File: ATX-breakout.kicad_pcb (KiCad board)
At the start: 2 copper layers, 67 x 59.5 mm, 27 parts, among them J1 I2C, J10 3V3 out, J11 12V out, J12 12V out, J2 EPS, J3 USB_A, J4 Raspberry_Pi_2_3, J5 ATX24pin, J6 12V out, J7 pson ext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

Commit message: added schematic PDF and updated BOM
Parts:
- R2: value 10K -> 10k
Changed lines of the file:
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@@
       (effects (font (size 1 1) (thickness 0.15)))
     )
-    (fp_text value 10K (at 3.81 2.37) (layer F.Fab)
+    (fp_text value 10k (at 3.81 2.37) (layer F.Fab)
       (effects (font (size 1 1) (thickness 0.15)))
     )

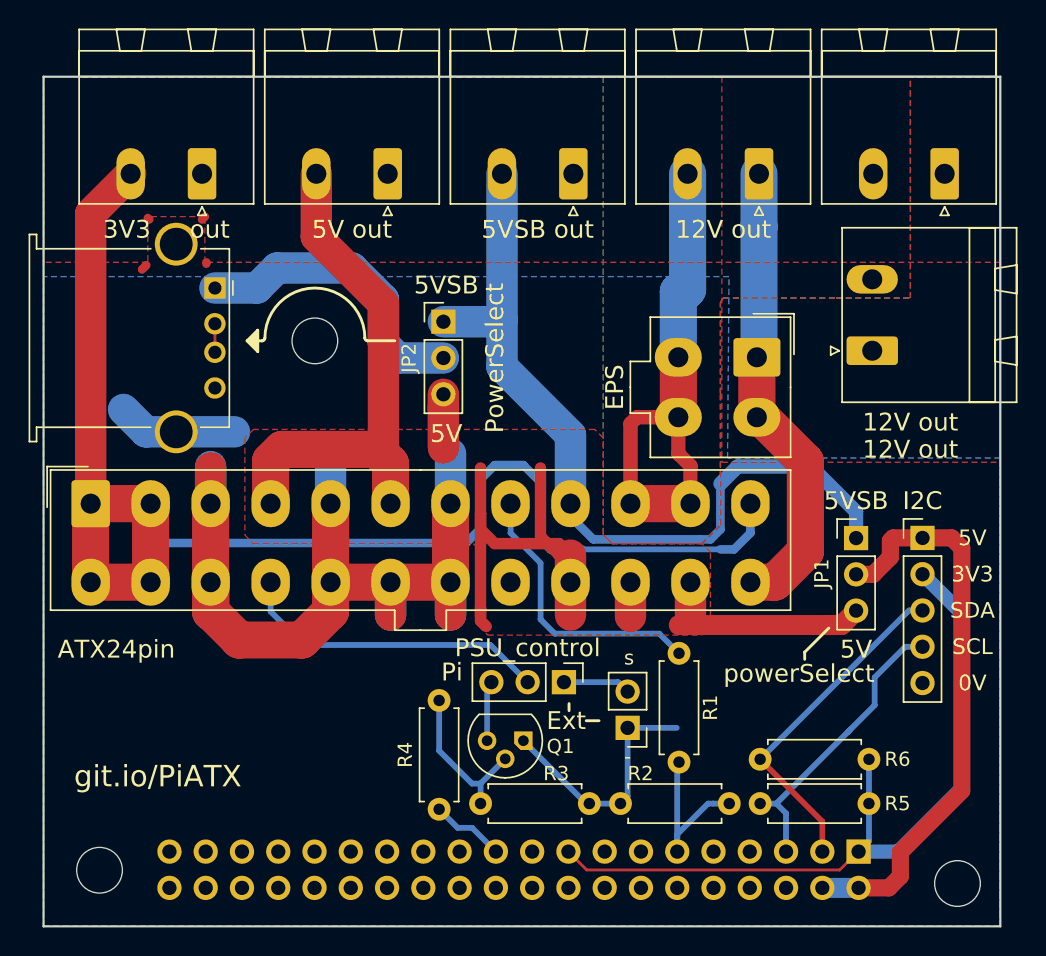
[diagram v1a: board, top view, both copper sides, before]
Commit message: rotated EPS and improved ground routing
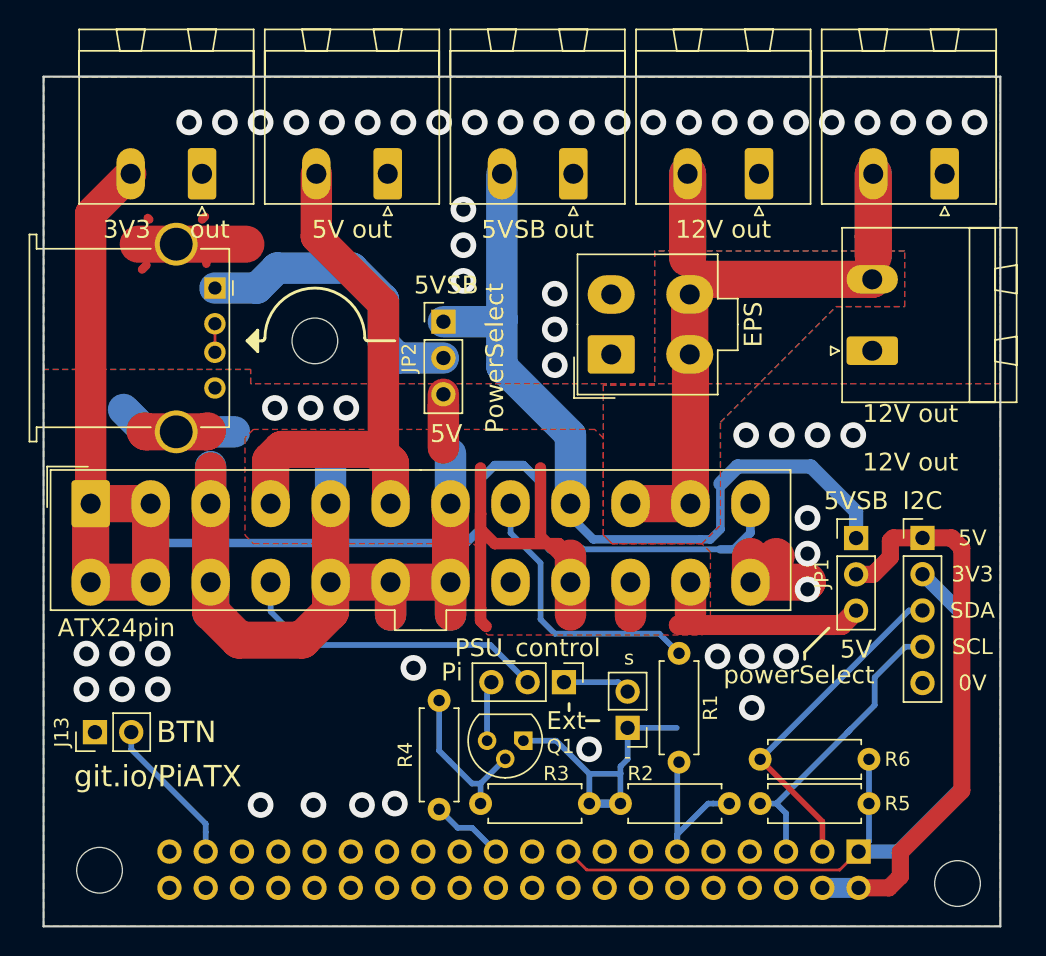
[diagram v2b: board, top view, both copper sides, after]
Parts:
- added J13: btn, Connector_PinHeader_2.54mm:PinHeader_1x02_P2.54mm_Vertical, F.Cu at (3.60, 45.9)
- moved J2 10.2 mm to (39.8, 19.4), turned to 90 degrees
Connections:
- J4 pad 37: (no net) -> Net-(J13-Pad2)
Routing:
- net +12V: track 37.4 -> 55.4 mm
- net Net-(J13-Pad2): track 0.00 -> 10.5 mm
- net GND: track 124.2 -> 115.1 mm, vias 0 -> 55
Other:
- board text added: "BTN"

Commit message: Updated silk screen and gerbers
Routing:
- net GND: vias 55 -> 54
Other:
- board text added: "GND"
- board text added: "PowerSelect USB"
- board text added: "powerSelect RPi"
- board text removed: "0V"
- board text removed: "PowerSelect"
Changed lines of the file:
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@@
   (general
     (thickness 1.6)
-    (drawings 61)
-    (tracks 275)
+    (drawings 74)
+    (tracks 274)
     (zones 0)
     (modules 28)
@@
       (effects (font (size 1 1) (thickness 0.15)))
     )
-    (fp_text value powerSelect (at -4 9.59 180) (layer F.SilkS)
+    (fp_text value powerSelect (at -4 9.59 180) (layer F.SilkS) hide
       (effects (font (size 1.25 1.25) (thickness 0.2)))
     )
@@
       (effects (font (size 1 1) (thickness 0.15)))
     )
-    (fp_text value "12V out" (at 2.4 -16.8 180) (layer F.SilkS)
+    (fp_text value "12V out" (at 2.4 -17.2 180) (layer F.SilkS)
       (effects (font (size 1.25 1.25) (thickness 0.2)))
     )
@@
       (effects (font (size 1 1) (thickness 0.15)))
     )
-    (fp_text value "12V out" (at -7.81 2.67 180) (layer F.SilkS)
+    (fp_text value "12V out" (at -6.36 2.62 180) (layer F.SilkS)
       (effects (font (size 1.25 1.25) (thickness 0.2)))
     )
@@
     )
   )
+  (gr_line (start 58.9 34.85) (end 58.9 32.3) (layer F.SilkS) (width 0.2))
+  (gr_line (start 54.9 34.85) (end 54.9 37.4) (layer F.SilkS) (width 0.2))
+  (gr_line (start 56.9 34.85) (end 58.9 34.85) (layer F.SilkS) (width 0.2))
+  (gr_line (start 58.9 32.3) (end 56.9 32.3) (layer F.SilkS) (width 0.2))
+  (gr_line (start 56.9 34.85) (end 54.9 34.85) (layer F.SilkS) (width 0.2))
+  (gr_line (start 54.9 37.4) (end 56.9 37.4) (layer F.SilkS) (width 0.2))
+  (gr_line (start 26 19.7) (end 26 22.25) (layer F.SilkS) (width 0.2))
+  (gr_line (start 28 19.7) (end 26 19.7) (layer F.SilkS) (width 0.2))
+  (gr_line (start 26 22.25) (end 28 22.25) (layer F.SilkS) (width 0.2))
+  (gr_line (start 30 17.15) (end 28 17.15) (layer F.SilkS) (width 0.2))
+  (gr_line (start 30 19.7) (end 30 17.15) (layer F.SilkS) (width 0.2))
+  (gr_line (start 28 19.7) (end 30 19.7) (layer F.SilkS) (width 0.2))
+  (gr_text "powerSelect\nRPi" (at 52.9 42.95) (layer F.SilkS)
+    (effects (font (size 1.25 1.25) (thickness 0.2)))
+  )
   (gr_text BTN (at 10 45.9) (layer F.SilkS)
     (effects (font (size 1.5 1.5) (thickness 0.3)))
@@
     (effects (font (size 1 1) (thickness 0.15)) (justify mirror))
   )
-  (gr_text 0V (at 65.048 42.46) (layer F.SilkS)
+  (gr_text GND (at 65.048 42.46) (layer F.SilkS)
     (effects (font (size 1.1 1.1) (thickness 0.18)))
   )
@@
     (effects (font (size 1.25 1.25) (thickness 0.2)))
   )
-  (gr_text PowerSelect (at 31.6 19.7 90) (layer F.SilkS)
+  (gr_text "PowerSelect\nUSB" (at 32.75 19.7 90) (layer F.SilkS)
     (effects (font (size 1.25 1.25) (thickness 0.2)))
   )
@@
   (via (at 51.7 25.1) (size 1.8) (drill 1) (layers F.Cu B.Cu) (net 3))
   (via (at 54.2 25.1) (size 1.8) (drill 1) (layers F.Cu B.Cu) (net 3))
-  (via (at 56.7 25.1) (size 1.8) (drill 1) (layers F.Cu B.Cu) (net 3))
   (segment (start 53.45 35.4) (end 53.5 35.35) (width 2.6) (layer F.Cu) (net 3))
   (segment (start 49.5 35.4) (end 53.45 35.4) (width 2.6) (layer F.Cu) (net 3))

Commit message: updated gerbers, silkscreen and renders
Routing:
- net GND: track 115.1 -> 124.0 mm
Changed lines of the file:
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@@
   (general
     (thickness 1.6)
-    (drawings 74)
-    (tracks 274)
+    (drawings 75)
+    (tracks 278)
     (zones 0)
     (modules 28)
@@
   )
   (setup
-    (last_trace_width 0.4)
+    (last_trace_width 2.6)
     (user_trace_width 0.4)
     (user_trace_width 0.6)
@@
     (descr "Through hole straight pin header, 1x03, 2.54mm pitch, single row")
     (tags "Through hole pin header THT 1x03 2.54mm single row")
-    (fp_text reference JP1 (at -2.4 2.49 90) (layer F.SilkS)
+    (fp_text reference JP1 (at -2.4 -0.21 90) (layer F.SilkS)
       (effects (font (size 1 1) (thickness 0.15)))
     )
@@
     (descr "Through hole straight pin header, 1x03, 2.54mm pitch, single row")
     (tags "Through hole pin header THT 1x03 2.54mm single row")
-    (fp_text reference JP2 (at -2.4 2.54 90) (layer F.SilkS)
+    (fp_text reference JP2 (at -2.4 -0.01 90) (layer F.SilkS)
       (effects (font (size 1 1) (thickness 0.15)))
     )
@@
       (effects (font (size 1 1) (thickness 0.15)))
     )
-    (fp_text value "12V out" (at -6.36 2.62 180) (layer F.SilkS)
+    (fp_text value "12V out" (at -6.56 2.62 180) (layer F.SilkS)
       (effects (font (size 1.25 1.25) (thickness 0.2)))
     )
@@
     )
   )
+  (gr_text git.io/PiATX (at 8 49) (layer B.SilkS)
+    (effects (font (size 1.5 1.5) (thickness 0.3)) (justify mirror))
+  )
   (gr_line (start 58.9 34.85) (end 58.9 32.3) (layer F.SilkS) (width 0.2))
   (gr_line (start 54.9 34.85) (end 54.9 37.4) (layer F.SilkS) (width 0.2))
@@
     (effects (font (size 1 1) (thickness 0.15)) (justify mirror))
   )
-  (gr_text "(64, 56.5)" (at 64 49.5 90) (layer B.SilkS)
+  (gr_text "(64, 56.5)" (at 62.6 52.5) (layer B.SilkS)
     (effects (font (size 1 1) (thickness 0.15)) (justify mirror))
   )
@@
   (via (at 29.4 9.3) (size 1.8) (drill 1) (layers F.Cu B.Cu) (net 3))
   (via (at 29.4 11.8) (size 1.8) (drill 1) (layers F.Cu B.Cu) (net 3))
-  (via (at 29.4 14.3) (size 1.8) (drill 1) (layers F.Cu B.Cu) (net 3))
   (via (at 49.2 25.1) (size 1.8) (drill 1) (layers F.Cu B.Cu) (net 3))
   (via (at 51.7 25.1) (size 1.8) (drill 1) (layers F.Cu B.Cu) (net 3))
@@
   (via (at 18.9 51) (size 1.8) (drill 1) (layers F.Cu B.Cu) (net 3))
   (via (at 15.2 51) (size 1.8) (drill 1) (layers F.Cu B.Cu) (net 3))
+  (via (at 26.9 11.8) (size 1.8) (drill 1) (layers F.Cu B.Cu) (net 3))
+  (segment (start 53.45 35.4) (end 53.5 35.35) (width 2.6) (layer B.Cu) (net 3))
+  (segment (start 49.5 35.4) (end 51.3 33.6) (width 2.6) (layer B.Cu) (net 3))
+  (segment (start 49.5 35.4) (end 53.45 35.4) (width 2.6) (layer B.Cu) (net 3))
+  (segment (start 49.5 35.4) (end 49.5 37.7) (width 2.6) (layer B.Cu) (net 3))
   (segment (start 41.1 29.9) (end 45.3 29.9) (width 2.6) (layer F.Cu) (net 4))
   (segment (start 45.3 19.5) (end 45.25 19.45) (width 2.6) (layer F.Cu) (net 4))

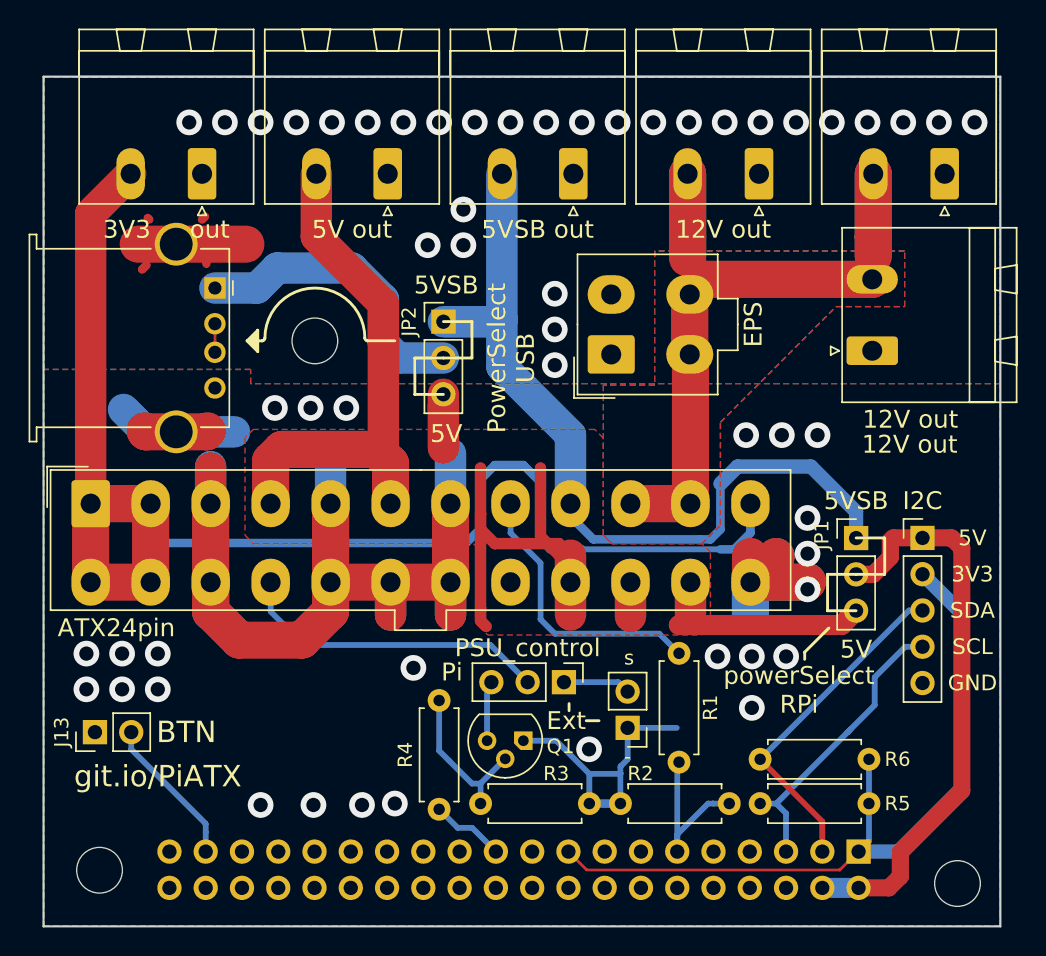
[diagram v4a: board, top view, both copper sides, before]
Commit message: Switched to vertical USB to clear pi ethernet jack
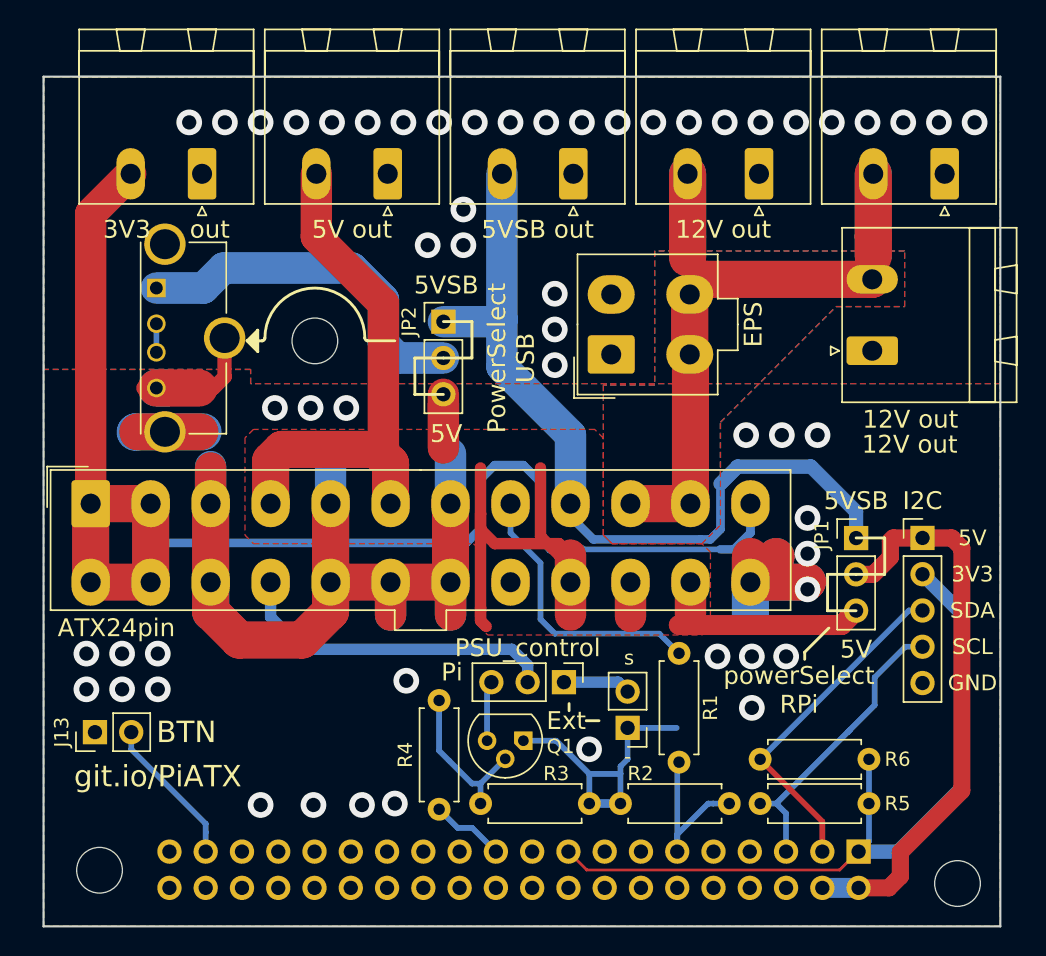
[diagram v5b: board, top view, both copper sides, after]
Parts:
- J3: value USB_A -> 1050570001; footprint Connector_USB:USB_A_Stewart_SS-52100-001_Horizontal -> Connector_USB:USB_A_Molex_105057_Vertical
- moved J3 4.10 mm to (7.90, 14.8)
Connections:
- J4 pad 10: (no net) -> Net-(J4-Pad10)
- J4 pad 12: (no net) -> Net-(J4-Pad12)
- J4 pad 13: (no net) -> Net-(J4-Pad13)
- J4 pad 15: (no net) -> Net-(J4-Pad15)
- J4 pad 16: (no net) -> Net-(J4-Pad16)
- J4 pad 18: (no net) -> Net-(J4-Pad18)
- J4 pad 19: (no net) -> Net-(J4-Pad19)
- J4 pad 22: (no net) -> Net-(J4-Pad22)
- J4 pad 23: (no net) -> Net-(J4-Pad23)
- J4 pad 24: (no net) -> Net-(J4-Pad24)
- J4 pad 26: (no net) -> Net-(J4-Pad26)
- J4 pad 27: (no net) -> Net-(J4-Pad27)
- J4 pad 28: (no net) -> Net-(J4-Pad28)
- J4 pad 29: (no net) -> Net-(J4-Pad29)
- J4 pad 31: (no net) -> Net-(J4-Pad31)
- J4 pad 32: (no net) -> Net-(J4-Pad32)
- J4 pad 33: (no net) -> Net-(J4-Pad33)
- J4 pad 35: (no net) -> Net-(J4-Pad35)
- J4 pad 36: (no net) -> Net-(J4-Pad36)
- J4 pad 38: (no net) -> Net-(J4-Pad38)
- J4 pad 40: (no net) -> Net-(J4-Pad40)
- J4 pad 7: (no net) -> Net-(J4-Pad7)
- J4 pad 8: (no net) -> Net-(J4-Pad8)
- J5 pad 20: (no net) -> Net-(J5-Pad20)
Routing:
- net Net-(J3-Pad1): track 21.0 -> 25.1 mm
- net GND: track 124.0 -> 122.3 mm
- net ~PS_ON: track 22.1 -> 23.0 mm
